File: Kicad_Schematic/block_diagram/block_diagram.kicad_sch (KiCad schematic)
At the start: 8 parts

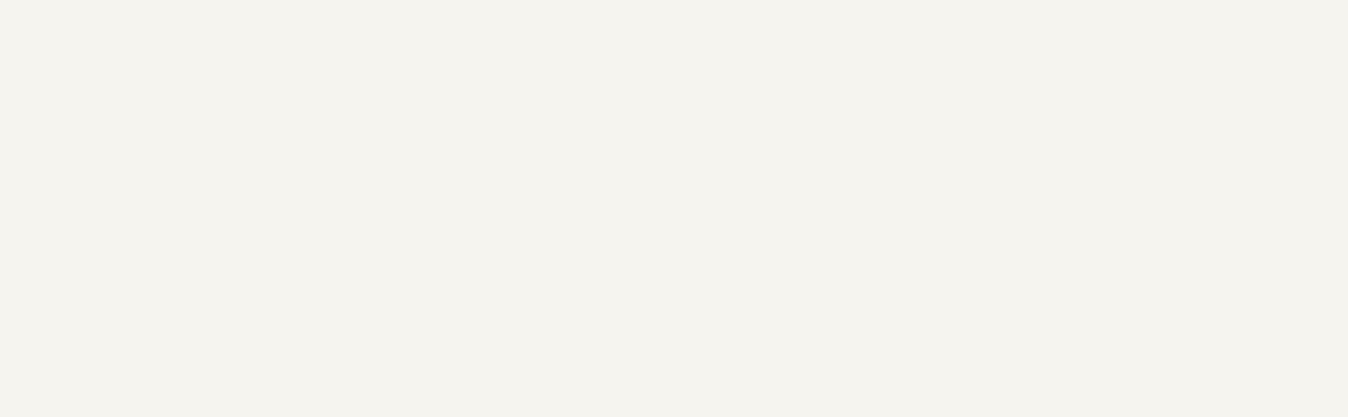
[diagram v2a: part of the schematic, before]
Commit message: Added sub-sheets for the detailed block diagrams
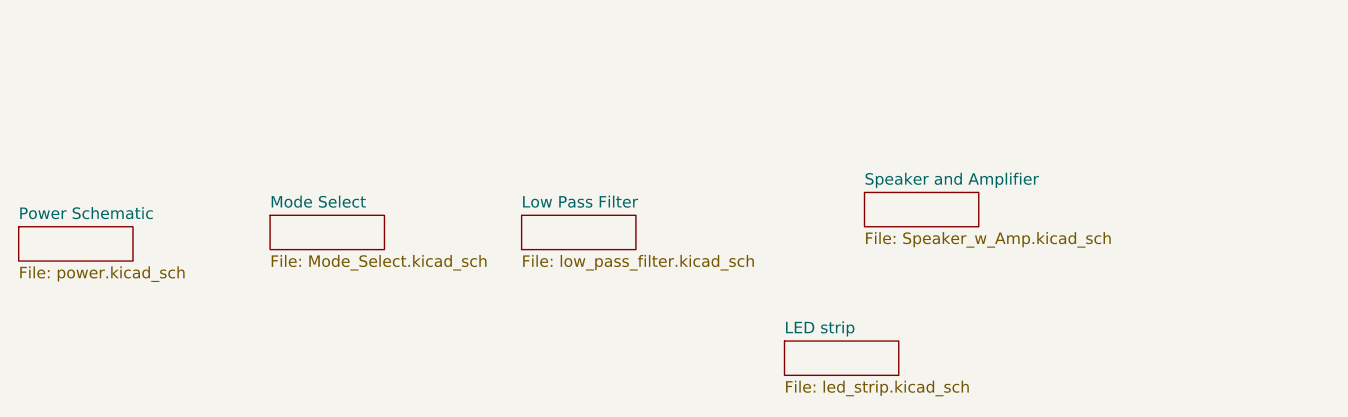
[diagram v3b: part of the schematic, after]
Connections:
- net at Low_Pass_Filter. (Output): now also Speaker_W_Amp. (Sound); no longer Pi_Pico. (3.3V)
- net at Speaker_W_Amp. (Sound): no longer Low_Pass_Filter. (Output)
- net at LEDs. (Light): now also Pi_Pico. (3.3V), Power. (5V), Speaker_W_Amp. (Sound)
- net at Pi_Pico. (3.3V): now also Microphone. (Digital_Out); no longer LEDs. (Light)
- net at Mode_Select. (Output_Mode): no longer Pi_Pico. (3.3V)
- net at Microphone. (Digital_Out): no longer Pi_Pico. (3.3V)
- new net: Low_Pass_Filter. (Output), Pi_Pico. (3.3V)
- new net: LEDs. (Light), Pi_Pico. (3.3V)
- new net: Mode_Select. (Output_Mode), Pi_Pico. (3.3V) (x2)
- new net: IMU. (Linear_Acceleration), Mode_Select. (Output_Mode), Pi_Pico. (3.3V)
- now unconnected: Mode_Select. (Output_Mode), Mode_Select. (Output_Mode), Power. (5V), Speaker_W_Amp. (Sound)
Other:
- added sheet LED strip (led_strip.kicad_sch)
- added sheet Low Pass Filter (low_pass_filter.kicad_sch)
- added sheet Mode Select (Mode_Select.kicad_sch)
- added sheet Power Schematic (power.kicad_sch)
- added sheet Speaker and Amplifier (Speaker_w_Amp.kicad_sch)
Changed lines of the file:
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@@
+		)
+	)
+	(sheet
+		(at 125.73 171.45)
+		(size 12.7 3.81)
+		(exclude_from_sim no)
+		(in_bom yes)
+		(on_board yes)
+		(dnp no)
+		(fields_autoplaced yes)
+		(stroke
+			(width 0.1524)
+			(type solid)
+		)
+		(fill
+			(color 0 0 0 0.0000)
+		)
+		(property "Sheetname" "Speaker and Amplifier"
+			(at 125.73 170.7384 0)
+			(effects
+				(font
+					(size 1.27 1.27)
+				)
+				(justify left bottom)
+			)
+		)
+		(property "Sheetfile" "Speaker_w_Amp.kicad_sch"
+			(at 125.73 175.8446 0)
+			(effects
+				(font
+					(size 1.27 1.27)
+				)
+				(justify left top)
+			)
+		)
+		(instances
+			(project "block_diagram"
+				(path "/7a474c3b-855e-4a89-97e9-3d42055b899d"
+					(page "5")
+				)
+			)
+		)
+	)
+	(sheet
+		(at 31.75 175.26)
+		(size 12.7 3.81)
+		(exclude_from_sim no)
+		(in_bom yes)
+		(on_board yes)
+		(dnp no)
+		(fields_autoplaced yes)
+		(stroke
+			(width 0.1524)
+			(type solid)
+		)
+		(fill
+			(color 0 0 0 0.0000)
+		)
+		(property "Sheetname" "Power Schematic"
+			(at 31.75 174.5484 0)
+			(effects
+				(font
+					(size 1.27 1.27)
+				)
+				(justify left bottom)
+			)
+		)
+		(property "Sheetfile" "power.kicad_sch"
+			(at 31.75 179.6546 0)
+			(effects
+				(font
+					(size 1.27 1.27)
+				)
+				(justify left top)
+			)
+		)
+		(instances
+			(project "block_diagram"
+				(path "/7a474c3b-855e-4a89-97e9-3d42055b899d"
+					(page "2")
+				)
+			)
+		)
+	)
+	(sheet
+		(at 116.84 187.96)
+		(size 12.7 3.81)
+		(exclude_from_sim no)
+		(in_bom yes)
+		(on_board yes)
+		(dnp no)
+		(fields_autoplaced yes)
+		(stroke
+			(width 0.1524)
+			(type solid)
+		)
+		(fill
+			(color 0 0 0 0.0000)
+		)
+		(property "Sheetname" "LED strip"
+			(at 116.84 187.2484 0)
+			(effects
+				(font
+					(size 1.27 1.27)
+				)
+				(justify left bottom)
+			)
+		)
+		(property "Sheetfile" "led_strip.kicad_sch"
+			(at 116.84 192.3546 0)
+			(effects
+				(font
+					(size 1.27 1.27)
+				)
+				(justify left top)
+			)
+		)
+		(instances
+			(project "block_diagram"
+				(path "/7a474c3b-855e-4a89-97e9-3d42055b899d"
+					(page "6")
+				)
+			)
+		)
+	)
+	(sheet
+		(at 59.69 173.99)
+		(size 12.7 3.81)
+		(exclude_from_sim no)
+		(in_bom yes)
+		(on_board yes)
+		(dnp no)
+		(fields_autoplaced yes)
+		(stroke
+			(width 0.1524)
+			(type solid)
+		)
+		(fill
+			(color 0 0 0 0.0000)
+		)
+		(property "Sheetname" "Mode Select"
+			(at 59.69 173.2784 0)
+			(effects
+				(font
+					(size 1.27 1.27)
+				)
+				(justify left bottom)
+			)
+		)
+		(property "Sheetfile" "Mode_Select.kicad_sch"
+			(at 59.69 178.3846 0)
+			(effects
+				(font
+					(size 1.27 1.27)
+				)
+				(justify left top)
+			)
+		)
+		(instances
+			(project "block_diagram"
+				(path "/7a474c3b-855e-4a89-97e9-3d42055b899d"
+					(page "3")
+				)
+			)
+		)
+	)
+	(sheet
+		(at 87.63 173.99)
+		(size 12.7 3.81)
+		(exclude_from_sim no)
+		(in_bom yes)
+		(on_board yes)
+		(dnp no)
+		(fields_autoplaced yes)
+		(stroke
+			(width 0.1524)
+			(type solid)
+		)
+		(fill
+			(color 0 0 0 0.0000)
+		)
+		(property "Sheetname" "Low Pass Filter"
+			(at 87.63 173.2784 0)
+			(effects
+				(font
+					(size 1.27 1.27)
+				)
+				(justify left bottom)
+			)
+		)
+		(property "Sheetfile" "low_pass_filter.kicad_sch"
+			(at 87.63 178.3846 0)
+			(effects
+				(font
+					(size 1.27 1.27)
+				)
+				(justify left top)
+			)
+		)
+		(instances
+			(project "block_diagram"
+				(path "/7a474c3b-855e-4a89-97e9-3d42055b899d"
+					(page "4")
+				)
+			)
 		)
 	)

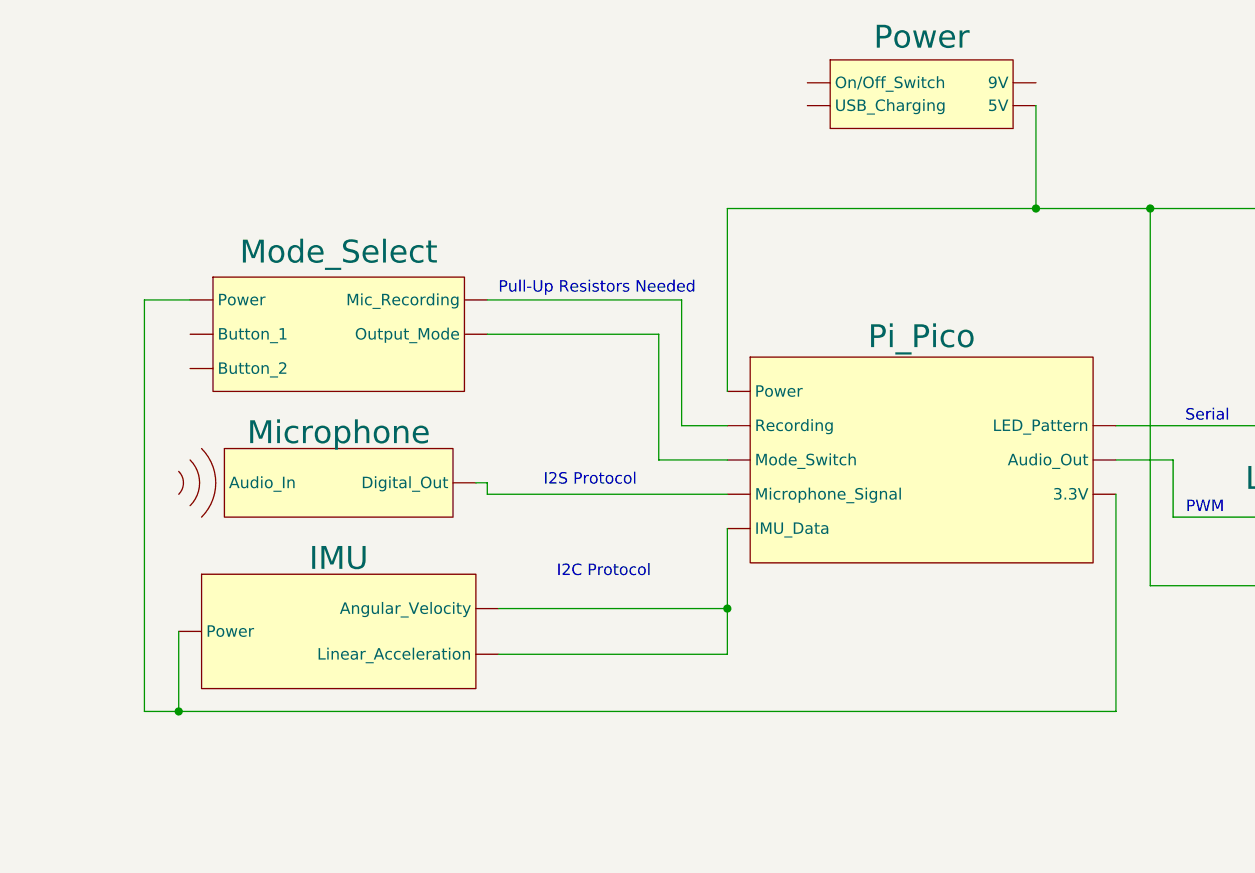
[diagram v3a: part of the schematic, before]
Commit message: Updated mode select block for a 3rd button
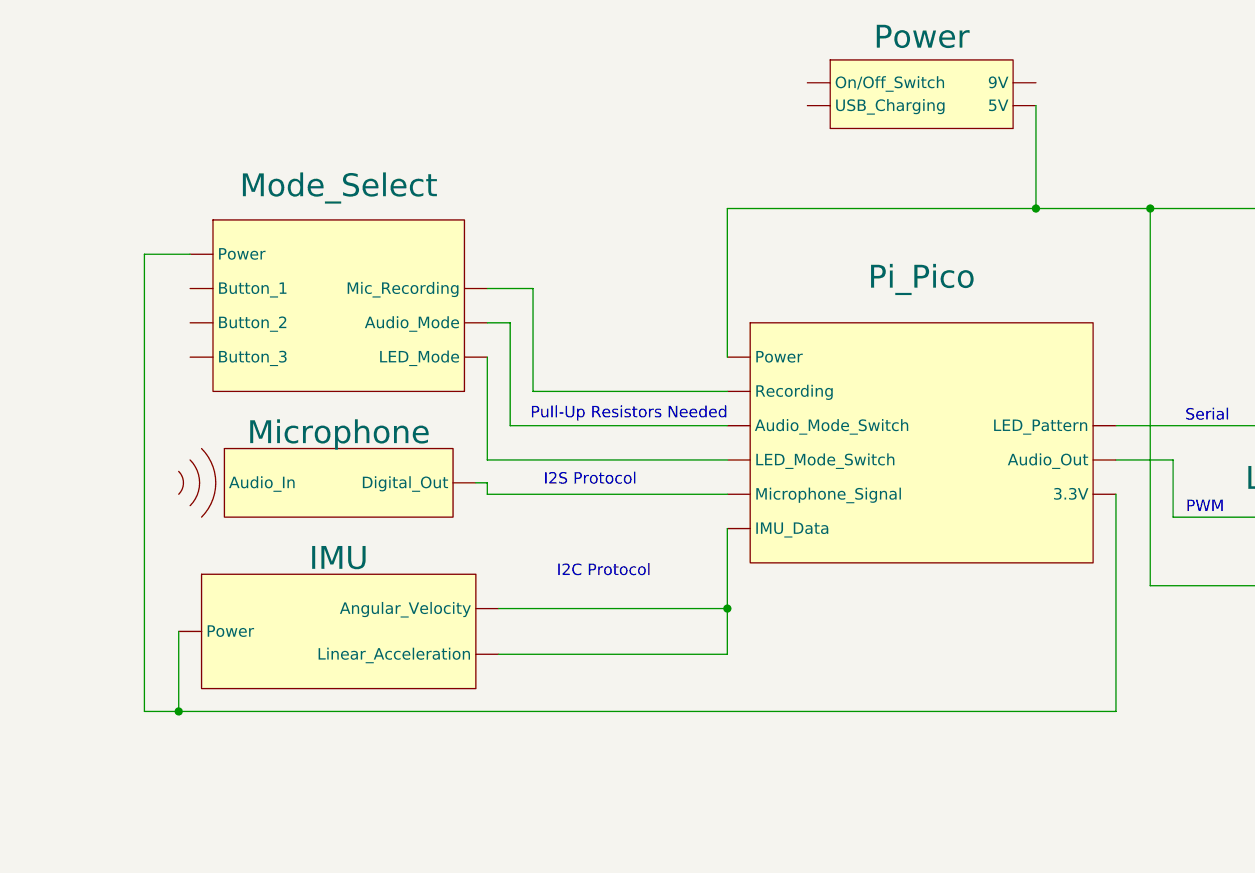
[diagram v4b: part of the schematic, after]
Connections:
- net at Low_Pass_Filter. (Output): now also Speaker_W_Amp. (Sound); no longer Pi_Pico. (3.3V)
- net at Speaker_W_Amp. (Sound): no longer Low_Pass_Filter. (Output)
- net at LEDs. (Light): now also Pi_Pico. (3.3V), Power. (5V), Speaker_W_Amp. (Sound)
- net at Pi_Pico. (3.3V): now also Microphone. (Digital_Out); no longer LEDs. (Light)
- net at Mode_Select. (LED_Mode): no longer Pi_Pico. (3.3V)
- net at Microphone. (Digital_Out): no longer Pi_Pico. (3.3V)
- new net: Low_Pass_Filter. (Output), Pi_Pico. (3.3V)
- new net: LEDs. (Light), Pi_Pico. (3.3V)
- new net: Mode_Select. (LED_Mode), Pi_Pico. (3.3V) (x3)
- new net: IMU. (Linear_Acceleration), Mode_Select. (LED_Mode), Pi_Pico. (3.3V)
- now unconnected: Mode_Select. (Output_Mode), Mode_Select. (Output_Mode), Power. (5V), Speaker_W_Amp. (Sound)
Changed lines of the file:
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@@
 	(text "Pull-Up Resistors Needed\n"
 		(exclude_from_sim no)
-		(at 96.012 83.82 0)
+		(at 99.568 97.79 0)
 		(effects
 			(font
@@
 	(wire
 		(pts
+			(xy 86.36 87.63) (xy 86.36 99.06)
+		)
+		(stroke
+			(width 0)
+			(type default)
+		)
+	)
+	(wire
+		(pts
 			(xy 160.02 102.87) (xy 153.67 102.87)
 		)
@@
 	(wire
 		(pts
-			(xy 45.72 85.09) (xy 45.72 130.81)
+			(xy 45.72 80.01) (xy 45.72 130.81)
 		)
 		(stroke
@@
 	(wire
 		(pts
-			(xy 83.82 85.09) (xy 105.41 85.09)
-		)
-		(stroke
-			(width 0)
-			(type default)
-		)
-	)
-	(wire
-		(pts
 			(xy 85.09 119.38) (xy 110.49 119.38)
 		)
@@
 	(wire
 		(pts
-			(xy 110.49 74.93) (xy 110.49 95.25)
-		)
-		(stroke
-			(width 0)
-			(type default)
-		)
-	)
-	(wire
-		(pts
-			(xy 102.87 88.9) (xy 102.87 102.87)
+			(xy 110.49 74.93) (xy 110.49 91.44)
+		)
+		(stroke
+			(width 0)
+			(type default)
+		)
+	)
+	(wire
+		(pts
+			(xy 83.82 102.87) (xy 110.49 102.87)
 		)
 		(stroke
@@
 	(wire
 		(pts
-			(xy 83.82 88.9) (xy 102.87 88.9)
-		)
-		(stroke
-			(width 0)
-			(type default)
-		)
-	)
-	(wire
-		(pts
-			(xy 105.41 85.09) (xy 105.41 99.06)
-		)
-		(stroke
-			(width 0)
-			(type default)
-		)
-	)
-	(wire
-		(pts
 			(xy 85.09 124.46) (xy 110.49 124.46)
 		)
@@
 	(wire
 		(pts
-			(xy 102.87 102.87) (xy 110.49 102.87)
-		)
-		(stroke
-			(width 0)
-			(type default)
-		)
-	)
-	(wire
-		(pts
 			(xy 83.82 105.41) (xy 83.82 106.68)
 		)
@@
 	(wire
 		(pts
+			(xy 86.36 99.06) (xy 110.49 99.06)
+		)
+		(stroke
+			(width 0)
+			(type default)
+		)
+	)
+	(wire
+		(pts
 			(xy 170.18 109.22) (xy 160.02 109.22)
 		)
@@
 	(wire
 		(pts
+			(xy 45.72 80.01) (xy 50.8 80.01)
+		)
+		(stroke
+			(width 0)
+			(type default)
+		)
+	)
+	(wire
+		(pts
 			(xy 144.78 74.93) (xy 157.48 74.93)
 		)
@@
 	(wire
 		(pts
+			(xy 83.82 87.63) (xy 86.36 87.63)
+		)
+		(stroke
+			(width 0)
+			(type default)
+		)
+	)
+	(wire
+		(pts
 			(xy 157.48 116.84) (xy 195.58 116.84)
 		)
@@
 	(wire
 		(pts
-			(xy 50.8 85.09) (xy 45.72 85.09)
-		)
-		(stroke
-			(width 0)
-			(type default)
-		)
-	)
-	(wire
-		(pts
 			(xy 83.82 106.68) (xy 110.49 106.68)
 		)
@@
 	(wire
 		(pts
-			(xy 105.41 99.06) (xy 110.49 99.06)
-		)
-		(stroke
-			(width 0)
-			(type default)
-		)
-	)
-	(wire
-		(pts
 			(xy 110.49 110.49) (xy 110.49 119.38)
 		)
@@
 	(wire
 		(pts
+			(xy 88.9 83.82) (xy 88.9 95.25)
+		)
+		(stroke
+			(width 0)
+			(type default)
+		)
+	)
+	(wire
+		(pts
 			(xy 110.49 119.38) (xy 110.49 124.46)
 		)
@@
 		(pts
 			(xy 153.67 106.68) (xy 153.67 130.81)
+		)
+		(stroke
+			(width 0)
+			(type default)
+		)
+	)
+	(wire
+		(pts
+			(xy 88.9 95.25) (xy 110.49 95.25)
+		)
+		(stroke
+			(width 0)
+			(type default)
+		)
+	)
+	(wire
+		(pts
+			(xy 83.82 91.44) (xy 83.82 102.87)
+		)
+		(stroke
+			(width 0)
+			(type default)
+		)
+	)
+	(wire
+		(pts
+			(xy 83.82 83.82) (xy 88.9 83.82)
 		)
 		(stroke
@@
 		(dnp no)
 		(property "Reference" "Pi_Pico"
-			(at 132.08 89.154 0)
+			(at 132.08 82.55 0)
 			(effects
 				(font
@@
 				(hide yes)
 			)
+		)
+		(pin ""
 		)
 		(pin ""
@@
 		(dnp no)
 		(property "Reference" "Mode_Select"
-			(at 67.31 79.756 0)
+			(at 67.31 72.39 0)
 			(effects
 				(font
@@
 		)
 		(property "Value" "~"
-			(at 67.31 81.28 0)
+			(at 67.31 74.93 0)
 			(effects
 				(font
@@
 		)
 		(pin ""
+		)
+		(pin ""
+		)
+		(pin ""
